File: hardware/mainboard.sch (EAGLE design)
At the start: 27 parts, among them IC1 ESP-12E/F, Q1 BC847BS, Q2 BC847BS, Q3 BC847BS

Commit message: Adding latest version of schematic
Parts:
- added C2: (opt), rcl:C-EUC1206
- added R16, R17, R19, R2, R5: 10k, rcl:R-EU_R1206
- added R18: 10k (opt), rcl:R-EU_R1206
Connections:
- net RITTO_MUTE renamed RITTO_MUTE_5V
- net RITTO_OPEN renamed RITTO_OPEN_5V
- removed net ESP12_RESET: IC1.IO16, IC1.RST, Q2A.C, Q2B.C, S1.1
- removed net GPIO_/FWUPLOAD: IC1.IO15, S2.15
- new net ESP12_/FWUPLOAD: IC1.IO0, R16.1, S2.15
- new net ESP12_/LED: IC1.IO2, R18.1
- new net ESP12_/RESET: IC1.IO16, IC1.RST, Q2A.C, Q2B.C, R2.1, S1.1
- new net GPIO_10_IN: IC1.IO10, R19.1, S2.14
- new net N$7: R17.2, S2.1
- net +3V3: now also C2.1, R16.2, R17.1, R18.2, R2.2, S2.3; no longer S2.1
- net GND: now also C2.2, R19.2, R5.2
- net GPIO_NO_RESET_ON_RING: now also IC1.IO9; no longer IC1.IO5
- net GPIO_RING_HOUSE_DETECT: now also IC1.IO5; no longer IC1.IO2
- net N$3: now also IC1.IO15, R5.1; no longer IC1.IO0
- net UART_RX: now also R6.1; no longer R3.1
- net UART_TX: now also R3.1; no longer R6.1
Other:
- note added: "ESP-12"
- note added: "Input/Output"
- note added: "Misc"
- moved on the sheet: C1, JP_UART, Q1A, Q1B, R1, R10, R11, R12, R3, R6, R7, R8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

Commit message: Replacing Vcc with V3.3
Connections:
- removed net VCC: IC1.VCC
- net +3V3: now also IC1.VCC
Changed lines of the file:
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@@
 <part name="P+1" library="supply1" library_urn="urn:adsk.eagle:library:371" deviceset="+24V" device=""/>
 <part name="GND2" library="supply1" library_urn="urn:adsk.eagle:library:371" deviceset="GND" device=""/>
-<part name="+3V1" library="supply1" library_urn="urn:adsk.eagle:library:371" deviceset="VCC" device=""/>
 <part name="R1" library="rcl" library_urn="urn:adsk.eagle:library:334" deviceset="R-EU_" device="R1206" package3d_urn="urn:adsk.eagle:package:23540/2" value="1k"/>
 <part name="+3V3" library="supply1" library_urn="urn:adsk.eagle:library:371" deviceset="+3V3" device=""/>
@@
 <part name="GND5" library="supply1" library_urn="urn:adsk.eagle:library:371" deviceset="GND" device=""/>
 <part name="IC1" library="esp-12e-f" deviceset="ESP-12E/F" device=""/>
-<part name="+3V6" library="supply1" library_urn="urn:adsk.eagle:library:371" deviceset="VCC" device=""/>
 <part name="GND7" library="supply1" library_urn="urn:adsk.eagle:library:371" deviceset="GND" device=""/>
 <part name="RITTO_SIGNAL" library="own_rast" deviceset="RAST_6" device=""/>
@@
 <part name="R19" library="rcl" library_urn="urn:adsk.eagle:library:334" deviceset="R-EU_" device="R1206" package3d_urn="urn:adsk.eagle:package:23540/2" value="10k"/>
 <part name="GND12" library="supply1" library_urn="urn:adsk.eagle:library:371" deviceset="GND" device=""/>
+<part name="+3V6" library="supply1" library_urn="urn:adsk.eagle:library:371" deviceset="+3V3" device=""/>
+<part name="+3V1" library="supply1" library_urn="urn:adsk.eagle:library:371" deviceset="+3V3" device=""/>
 </parts>
 <sheets>
@@
 <attribute name="VALUE" x="-73.66" y="45.72" size="1.778" layer="96"/>
 </instance>
-<instance part="+3V1" gate="VCC" x="-55.88" y="78.74" smashed="yes">
-<attribute name="VALUE" x="-58.42" y="73.66" size="1.778" layer="96" rot="R90"/>
-</instance>
 <instance part="R1" gate="G$1" x="-20.32" y="-81.28" smashed="yes">
 <attribute name="NAME" x="-24.13" y="-79.7814" size="1.778" layer="95"/>
@@
 <attribute name="NAME" x="50.8" y="78.74" size="2.54" layer="95"/>
 <attribute name="VALUE" x="50.8" y="73.66" size="2.54" layer="96"/>
-</instance>
-<instance part="+3V6" gate="VCC" x="27.94" y="12.7" smashed="yes" rot="R180">
-<attribute name="VALUE" x="30.48" y="17.78" size="1.778" layer="96" rot="R270"/>
 </instance>
 <instance part="GND7" gate="1" x="111.76" y="15.24" smashed="yes">
@@
 <instance part="GND12" gate="1" x="17.78" y="71.12" smashed="yes" rot="R180">
 <attribute name="VALUE" x="20.32" y="73.66" size="1.778" layer="96" rot="R180"/>
+</instance>
+<instance part="+3V6" gate="G$1" x="27.94" y="12.7" smashed="yes" rot="R180">
+<attribute name="VALUE" x="30.48" y="17.78" size="1.778" layer="96" rot="R270"/>
+</instance>
+<instance part="+3V1" gate="G$1" x="-55.88" y="78.74" smashed="yes">
+<attribute name="VALUE" x="-58.42" y="73.66" size="1.778" layer="96" rot="R90"/>
 </instance>
 </instances>
@@
 <net name="+3V3" class="0">
 <segment>
-<pinref part="+3V1" gate="VCC" pin="VCC"/>
 <pinref part="U1" gate="G$1" pin="VOUT"/>
-<wire x1="-55.88" y1="76.2" x2="-55.88" y2="66.04" width="0.1524" layer="91"/>
 <pinref part="C1" gate="G$1" pin="1"/>
 <wire x1="-55.88" y1="66.04" x2="-55.88" y2="63.5" width="0.1524" layer="91"/>
@@
 <pinref part="C2" gate="G$1" pin="1"/>
 <wire x1="-45.72" y1="66.04" x2="-45.72" y2="63.5" width="0.1524" layer="91"/>
+<pinref part="+3V1" gate="G$1" pin="+3V3"/>
+<wire x1="-55.88" y1="76.2" x2="-55.88" y2="66.04" width="0.1524" layer="91" style="longdash"/>
 </segment>
 <segment>
@@
 <pinref part="+3V9" gate="G$1" pin="+3V3"/>
 <wire x1="-20.32" y1="48.26" x2="-20.32" y2="35.56" width="0.1524" layer="91"/>
+</segment>
+<segment>
+<pinref part="IC1" gate="G$1" pin="VCC"/>
+<wire x1="45.72" y1="20.32" x2="27.94" y2="20.32" width="0.1524" layer="91"/>
+<pinref part="+3V6" gate="G$1" pin="+3V3"/>
+<wire x1="27.94" y1="15.24" x2="27.94" y2="20.32" width="0.1524" layer="91" style="longdash"/>
 </segment>
 </net>
@@
 </segment>
 </net>
-<net name="VCC" class="0">
-<segment>
-<pinref part="IC1" gate="G$1" pin="VCC"/>
-<wire x1="45.72" y1="20.32" x2="27.94" y2="20.32" width="0.1524" layer="91"/>
-<pinref part="+3V6" gate="VCC" pin="VCC"/>
-<wire x1="27.94" y1="20.32" x2="27.94" y2="15.24" width="0.1524" layer="91"/>
-</segment>
-</net>

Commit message: Checkpoint commit for board file
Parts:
- removed R9*, R9*1: 0 (opt), rcl:R-EU_R1206
- added R22, R23: 0 (opt), rcl:R-EU_R1206
- renumbered S1 to RESET, WPS_BTN to WPS
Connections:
- removed net N$12: Q2A.B, R13.2
- removed net N$13: Q2B.B, R4.1
- new net N$8: Q2B.B, R4.2
- new net N$9: Q2A.B, R13.1
- net GPIO_RING_HOME_DETECT: now also R13.2, R22.2; no longer R13.1, R9*1.2
- net GPIO_RING_HOUSE_DETECT: now also R23.2, R4.1; no longer R4.2, R9*.2
- net N$5: now also R23.1; no longer R9*.1
- net N$6: now also R22.1; no longer R9*1.1
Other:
- moved on the sheet: C1, C2, R13, R4, U1

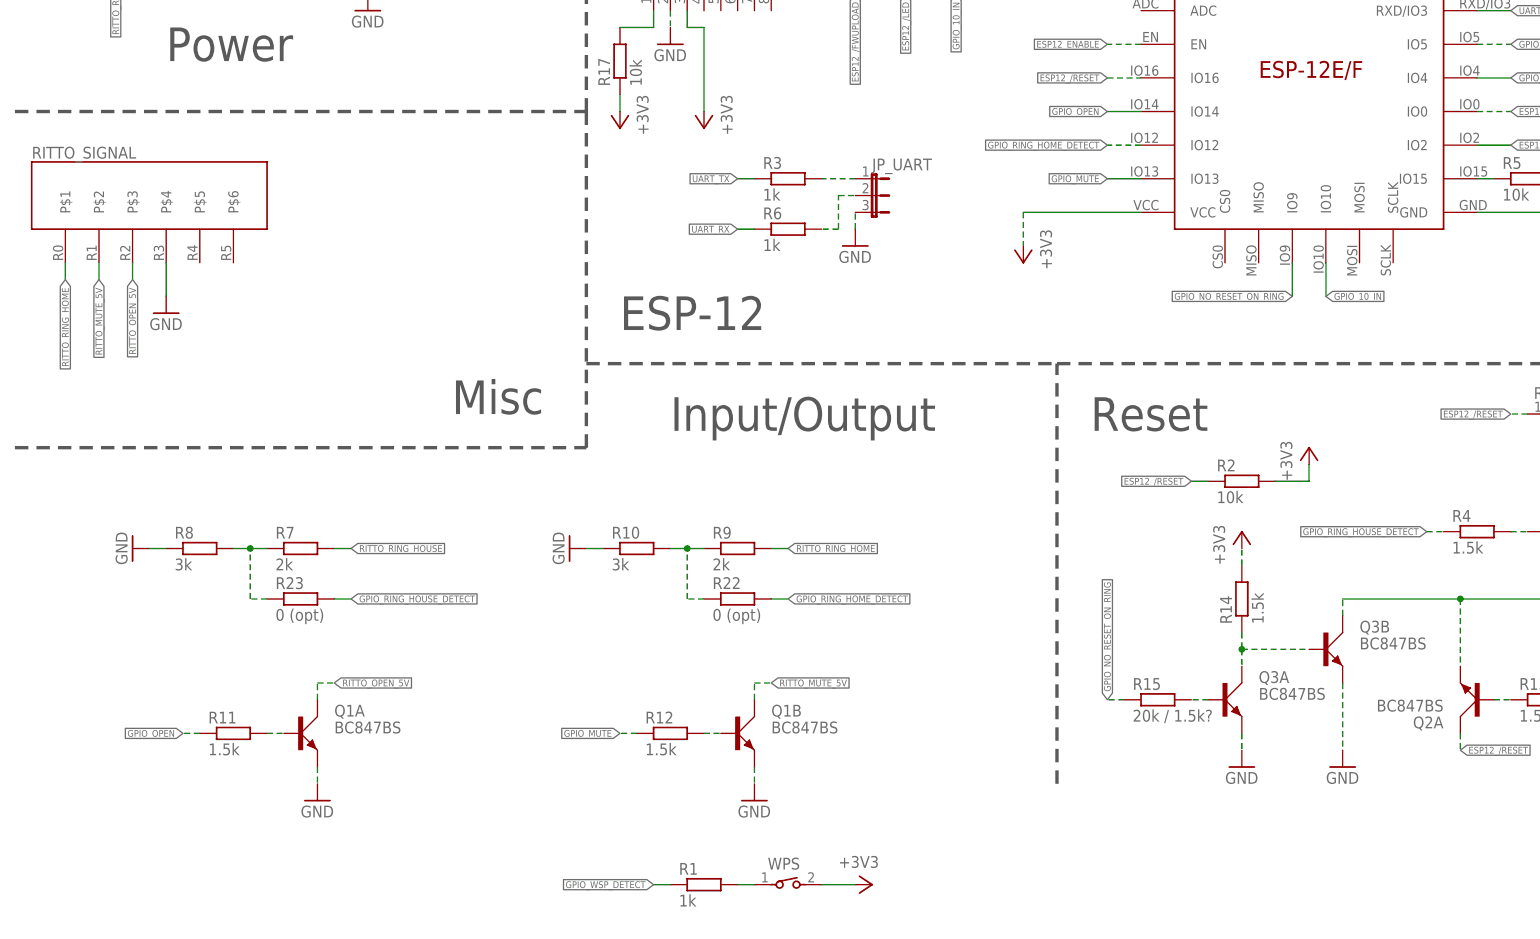
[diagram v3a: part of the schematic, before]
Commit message: Adding USB/FTDI
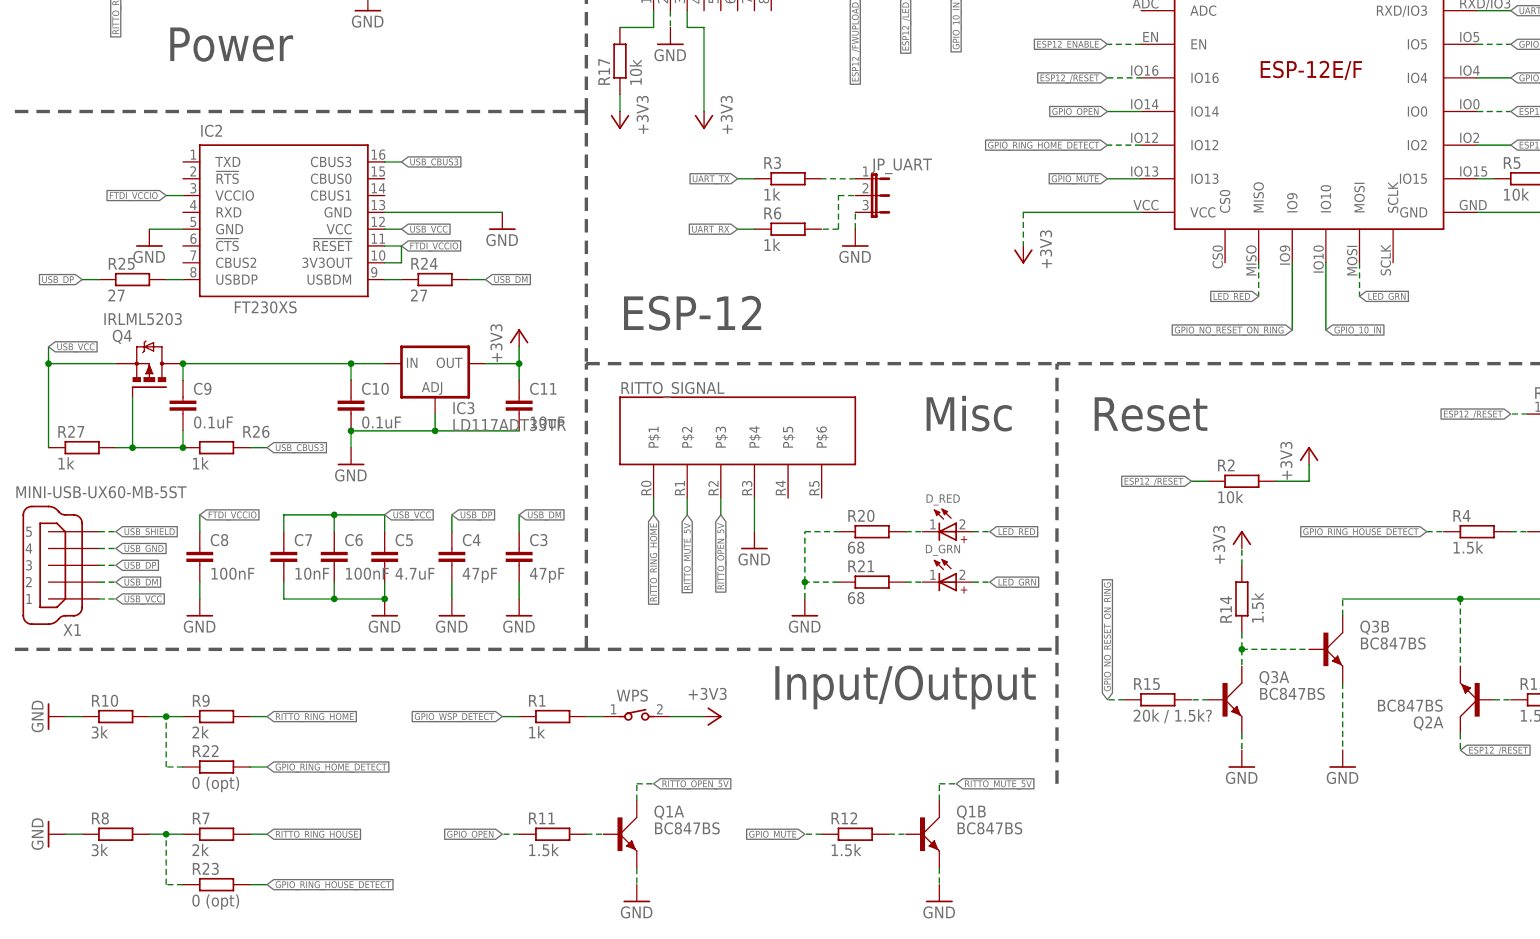
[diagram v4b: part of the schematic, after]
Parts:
- added C10, C9: 0.1uF, rcl:C-EUC1206
- added C11: 10uF, rcl:C-EUC1206
- added C3, C4: 47pF, rcl:C-EUC1206
- added C5: 4.7uF, rcl:C-EUC1206
- added C6, C8: 100nF, rcl:C-EUC1206
- added C7: 10nF, rcl:C-EUC1206
- added D_GRN: (no value), 156120RS75300_Eagle_WL-SMRW_rev20b:WL-SMRW_1206_CYL_156120VS75300_NOR
- added D_RED: (no value), 156120RS75300_Eagle_WL-SMRW_rev20b:WL-SMRW_1206_CYL_156120RS75300_NOR
- added IC2: FT230XS, ftdichip:FT230XS
- added IC3: LD117ADT33TR, v-reg:LD117ADT33TR
- added Q4: IRLML5203, transistor-power:IRLML5203
- added R20, R21: 68, rcl:R-EU_R1206
- added R24, R25: 27, rcl:R-EU_R1206
- added R26, R27: 1k, rcl:R-EU_R1206
- added X1: MINI-USB-UX60-MB-5ST, con-hirose:MINI-USB-UX60-MB-5ST
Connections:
- new net FTDI_VCCIO: C8.1, IC2.!RESET, IC2.3V3OUT, IC2.VCCIO
- new net LED_GRN: D_GRN.+, IC1.MOSI
- new net LED_RED: D_RED.+, IC1.MISO
- new net N$12: D_RED.-, R20.2
- new net N$13: D_GRN.-, R21.2
- new net N$17: IC2.USBDM, R24.1
- new net N$18: C9.2, Q4.G, R26.1, R27.2
- new net N$19: IC2.USBDP, R25.2
- new net N$20: C10.1, C9.1, IC3.IN, Q4.D
- new net USB_CBUS3: IC2.CBUS3, R26.2
- new net USB_DM: C3.1, R24.2, X1.2
- new net USB_DP: C4.1, R25.1, X1.3
- new net USB_GND: X1.4
- new net USB_SHIELD: X1.5
- new net USB_VCC: C5.1, C6.1, C7.1, IC2.VCC, Q4.S, R27.1, X1.1
- net +3V3: now also C11.1, IC3.OUT
- net GND: now also C10.2, C11.2, C3.2, C4.2, C5.2, C6.2, C7.2, C8.2, IC2.GND, IC2.GND@1, IC3.ADJ, R20.1, R21.1
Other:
- moved on the sheet: Q1A, Q1B, R1, R10, R11, R12, R22, R23, R7, R8, R9, RITTO_SIGNAL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

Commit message: Checkpoint commit layout
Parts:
- added R28, R29: 10k, rcl:R-EU_R1206
- renumbered JP_UART to UART
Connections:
- new net N$21: IC2.RXD, R28.2
- new net N$22: IC2.!CTS, R29.2
- net FTDI_VCCIO: now also R28.1, R29.1
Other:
- moved on the sheet: IC2, R24, R25

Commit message: Finalizing board file
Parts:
- added 3V3, GND, HSE: TPTP10SQ, testpad:TPTP10SQ
- renumbered RITTO_PWR to PWR, RITTO_SIGNAL to SIGNAL
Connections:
- removed net USB_GND: X1.4
- net +3V3: now also 3V3.TP
- net GND: now also GND.TP, X1.4
- net RITTO_RING_HOUSE: now also HSE.TP
